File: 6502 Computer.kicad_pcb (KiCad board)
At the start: 2 copper layers, 7 parts, among them SW1 CK_KMS2xxG, U1 6502, U2 MK4164N, U3 PL611-01-xxxT, U4 2764, U5 6522, U6 LCD-016N002L

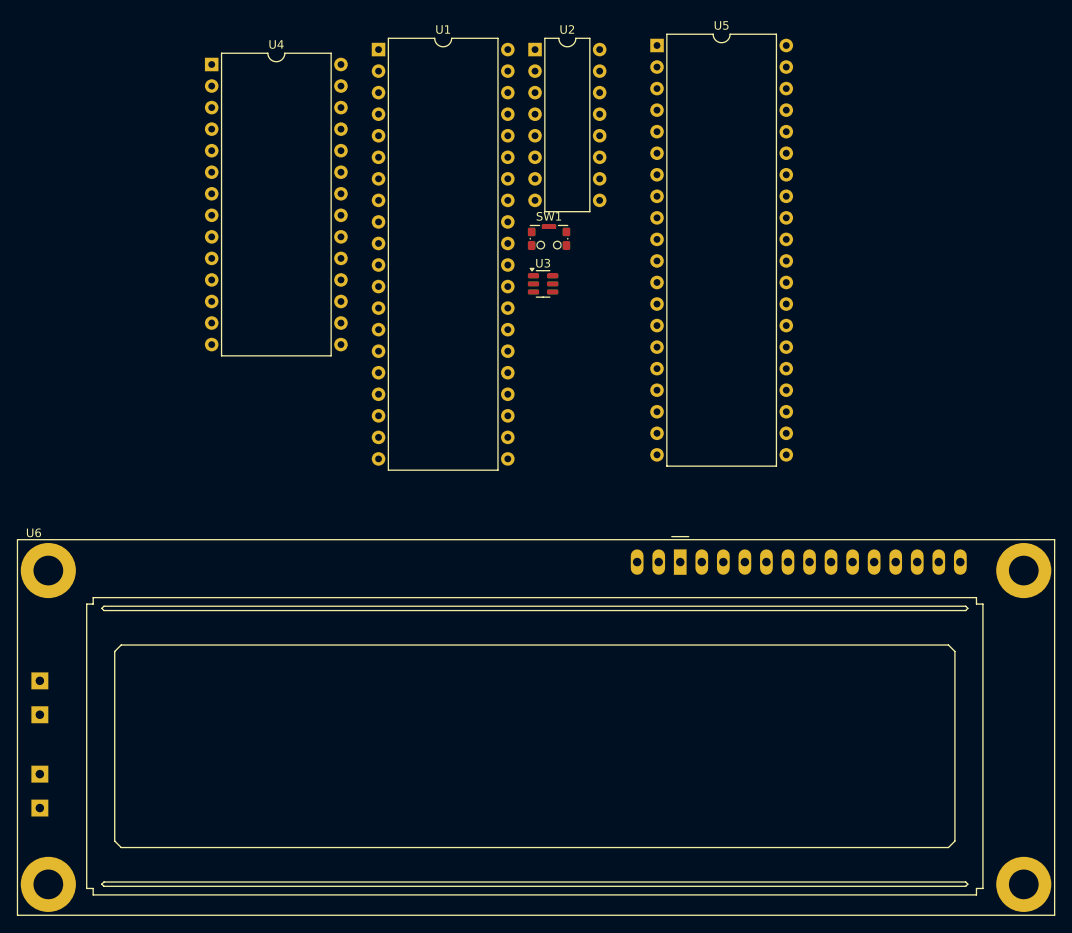
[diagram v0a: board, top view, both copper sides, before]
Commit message: Finished creating debug board and sent for manufacturing
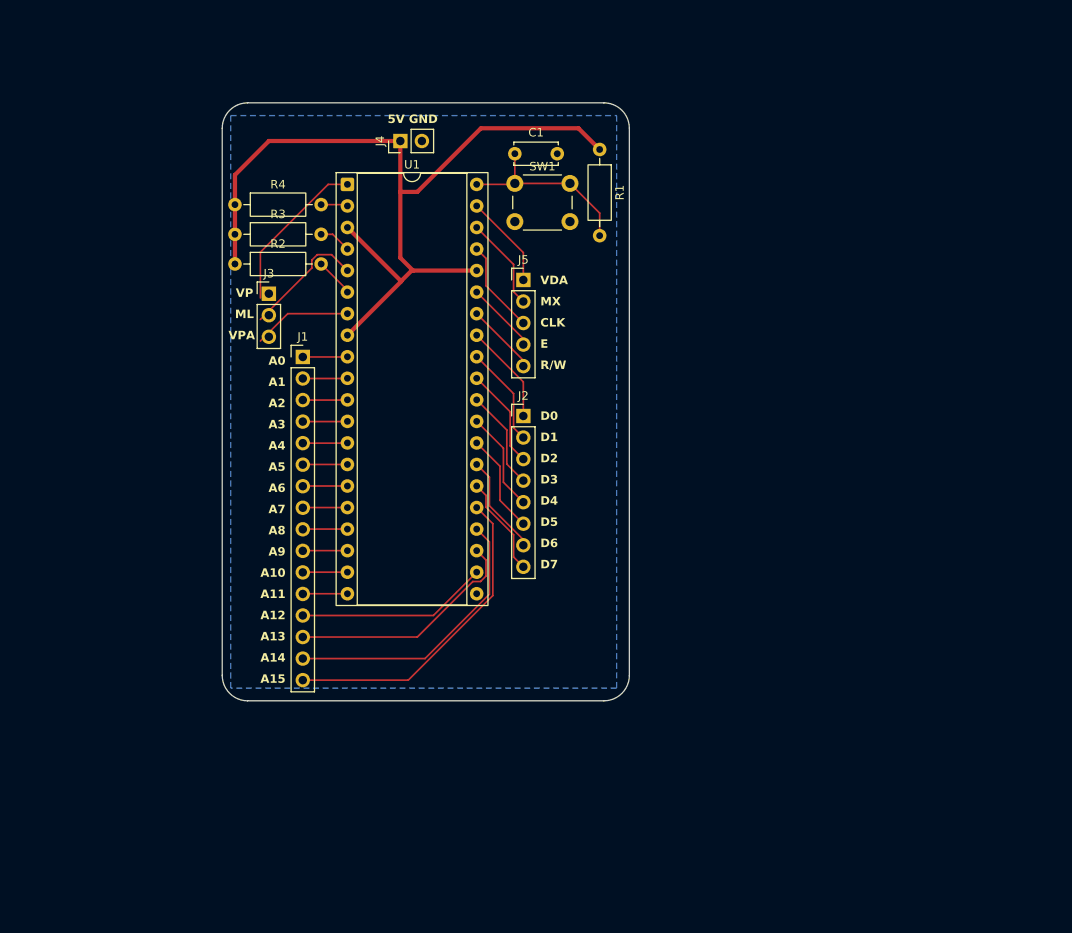
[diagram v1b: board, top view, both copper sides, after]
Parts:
- removed U2: MK4164N, Package_DIP:DIP-16_W7.62mm
- removed U3: PL611-01-xxxT, Package_TO_SOT_SMD:SOT-23-6
- removed U4: 2764, Package_DIP:DIP-28_W15.24mm
- removed U5: 6522, Package_DIP:DIP-40_W15.24mm
- removed U6: LCD-016N002L, Display:LCD-016N002L
- added C1: 1u, Capacitor_THT:C_Disc_D5.0mm_W2.5mm_P5.00mm, F.Cu at (130.5, 68.0)
- added J1: Conn_01x16_Pin, Connector_PinHeader_2.54mm:PinHeader_1x16_P2.54mm_Vertical, F.Cu at (105.5, 92.0)
- added J2: Conn_01x08_Pin, Connector_PinHeader_2.54mm:PinHeader_1x08_P2.54mm_Vertical, F.Cu at (131.5, 98.9)
- added J3: Conn_01x03_Pin, Connector_PinHeader_2.54mm:PinHeader_1x03_P2.54mm_Vertical, F.Cu at (101.5, 84.5)
- added J4: Conn_01x02_Pin, Connector_PinHeader_2.54mm:PinHeader_1x02_P2.54mm_Vertical, F.Cu at (117.0, 66.5)
- added J5: Conn_01x05_Pin, Connector_PinHeader_2.54mm:PinHeader_1x05_P2.54mm_Vertical, F.Cu at (131.5, 82.9)
- added R1: 10k, Resistor_THT:R_Axial_DIN0207_L6.3mm_D2.5mm_P10.16mm_Horizontal, F.Cu at (140.5, 67.5)
- added R2: 3.3k, Resistor_THT:R_Axial_DIN0207_L6.3mm_D2.5mm_P10.16mm_Horizontal, F.Cu at (97.5, 81.0)
- added R3: 3.3k, Resistor_THT:R_Axial_DIN0207_L6.3mm_D2.5mm_P10.16mm_Horizontal, F.Cu at (97.5, 77.5)
- added R4: 3.3k, Resistor_THT:R_Axial_DIN0207_L6.3mm_D2.5mm_P10.16mm_Horizontal, F.Cu at (97.5, 74.0)
- SW1: value CK_KMS2xxG -> SW_Push; footprint Button_Switch_SMD:SW_SPST_CK_KMS2xxGP -> Button_Switch_THT:SW_PUSH_6mm_H5mm
- U1: value 6502 -> W65C816SxP; footprint Package_DIP:DIP-40_W15.24mm -> Package_DIP:DIP-40_W15.24mm_Socket
- moved U1 16.3 mm to (110.8, 71.6)
- moved SW1 7.66 mm to (130.5, 71.5)
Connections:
- SW1 pad 1: GND -> RESET
- SW1 pad 2: +5V -> GND
- U1 pad 1: GND -> VP
- U1 pad 10: Net-(U1-A1) -> A1
- U1 pad 11: Net-(U1-A2) -> A2
- U1 pad 12: Net-(U1-A3) -> A3
- U1 pad 13: Net-(U1-A4) -> A4
- U1 pad 14: Net-(U1-A5) -> A5
- U1 pad 15: Net-(U1-A6) -> A6
- U1 pad 16: Net-(U1-A0) -> A7
- U1 pad 17: Net-(U1-A8) -> A8
- U1 pad 18: Net-(U1-A9) -> A9
- U1 pad 19: Net-(U1-A10) -> A10
- U1 pad 2: +5V -> Net-(U1-RDY)
- U1 pad 20: unconnected-(U1-A11-Pad20) -> A11
- U1 pad 22: unconnected-(U1-A12-Pad22) -> A12
- U1 pad 23: unconnected-(U1-A13-Pad23) -> A13
- U1 pad 24: unconnected-(U1-A14-Pad24) -> A14
- U1 pad 25: unconnected-(U1-A15-Pad25) -> A15
- U1 pad 26: unconnected-(U1-D7-Pad26) -> D7
- U1 pad 27: unconnected-(U1-D6-Pad27) -> D6
- U1 pad 28: unconnected-(U1-D5-Pad28) -> D5
- U1 pad 29: unconnected-(U1-D4-Pad29) -> D4
- U1 pad 3: unconnected-(U1-ϕ1-Pad3) -> +5V
- U1 pad 30: unconnected-(U1-D3-Pad30) -> D3
- U1 pad 31: unconnected-(U1-D2-Pad31) -> D2
- U1 pad 32: unconnected-(U1-D1-Pad32) -> D1
- U1 pad 33: GND -> D0
- U1 pad 34: unconnected-(U1-R/~{W}-Pad34) -> R/W
- U1 pad 35: unconnected-(U1-nc-Pad35) -> E
- U1 pad 36: unconnected-(U1-nc-Pad36) -> +5V
- U1 pad 37: unconnected-(U1-ϕ0-Pad37) -> CLK
- U1 pad 38: unconnected-(U1-~{SO}-Pad38) -> MX
- U1 pad 39: unconnected-(U1-ϕ2-Pad39) -> VDA
- U1 pad 4: unconnected-(U1-~{IRQ}-Pad4) -> Net-(U1-~{IRQ})
- U1 pad 40: Net-(SW1-B) -> RESET
- U1 pad 5: unconnected-(U1-nc-Pad5) -> ML
- U1 pad 6: unconnected-(U1-~{NMI}-Pad6) -> Net-(U1-~{NMI})
- U1 pad 7: Net-(U1-SYNC) -> VPA
- U1 pad 9: Net-(U1-A0) -> A0
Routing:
- net +5V: track 0.00 -> 102.6 mm
- net A15: track 0.00 -> 37.7 mm
- net A14: track 0.00 -> 33.4 mm
- net A13: track 0.00 -> 28.0 mm
- net A12: track 0.00 -> 22.6 mm
- net RESET: track 0.00 -> 22.2 mm
- net VP: track 0.00 -> 19.0 mm
- net ML: track 0.00 -> 14.7 mm
- net D5: track 0.00 -> 11.8 mm
- net D2: track 0.00 -> 11.8 mm
- net D0: track 0.00 -> 11.8 mm
- net D3: track 0.00 -> 11.8 mm
- net D7: track 0.00 -> 11.8 mm
- net D1: track 0.00 -> 11.8 mm
- net D4: track 0.00 -> 11.8 mm
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- added copper zone on B.Cu, net GND
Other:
- board outline added: 48 x 70.5 mm
- board text added: "5V"
- board text added: "A0"
- board text added: "A1"
- board text added: "A10"
- board text added: "A11"
- board text added: "A12"
- board text added: "A13"
- board text added: "A14"
- board text added: "A15"
- board text added: "A2"
- board text added: "A3"
- board text added: "A4"
- board text added: "A5"
- board text added: "A6"
- board text added: "A7"
- board text added: "A8"
- board text added: "A9"
- board text added: "CLK"
- board text added: "D0"
- board text added: "D1"
- board text added: "D2"
- board text added: "D3"
- board text added: "D4"
- board text added: "D5"
- board text added: "D6"
- board text added: "D7"
- board text added: "E"
- board text added: "GND"
- board text added: "ML"
- board text added: "MX"
- board text added: "R/W"
- board text added: "VDA"
- board text added: "VP"
- board text added: "VPA"
